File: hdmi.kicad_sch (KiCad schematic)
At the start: 46 parts, among them Q3 NVJD4401NT1G, U15 TPD4E05U06QDQARQ1, U17 TPD4E05U06QDQARQ1, U18 TPD4E05U06QDQARQ1, U21 SN75DP159_VQFN, U22 SN74AVC2T245_UQFN, U23 SN74LVC1T45YZPR, U25 NTS0104UK

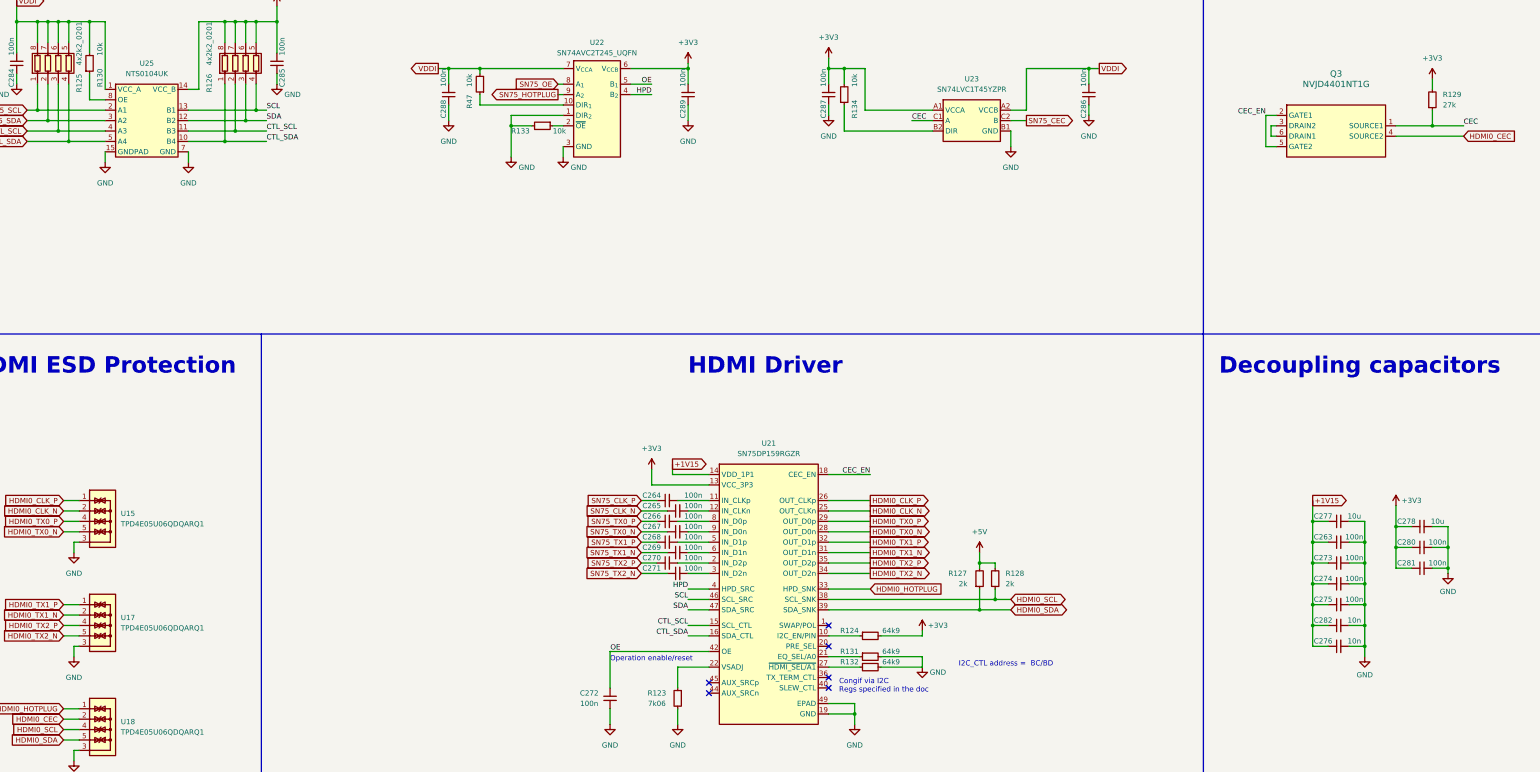
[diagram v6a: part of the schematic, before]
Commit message: [#54899] Clean duplicated components
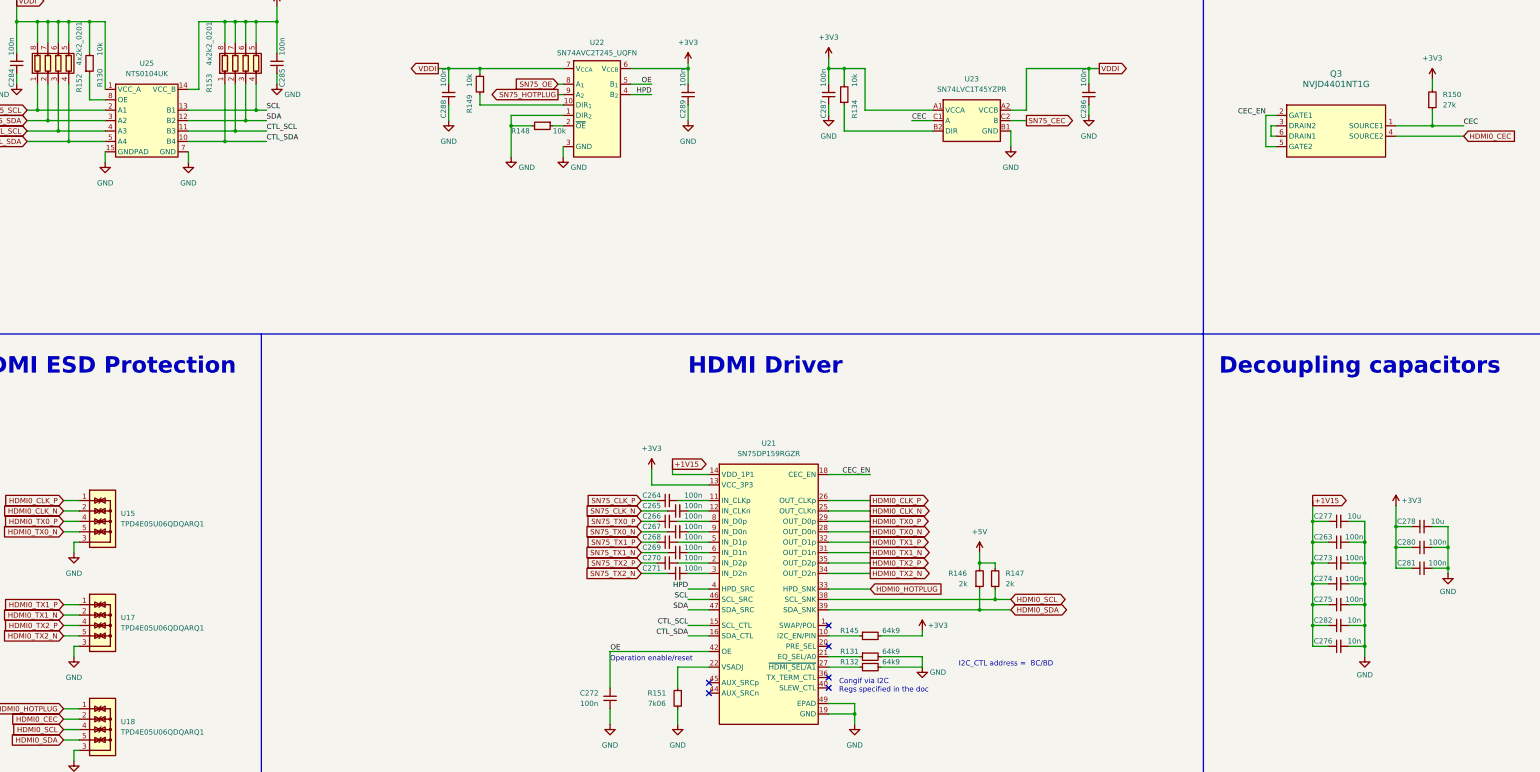
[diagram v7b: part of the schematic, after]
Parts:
- removed R123: 7k06, antmicro-footprints:R_0402_1005Metric, symbol antmicroResistors0402:R_7k06_0402
- removed R124: R_64k9_0402, antmicro-footprints:R_0402_1005Metric, symbol antmicroResistors0402:R_64k9_0402
- removed R125, R126: R_4x2k2_0201_array, antmicro-footprints:R_Array_4x0201_Panasonic_EXB18V, symbol antmicroResistorNetworksArrays:R_4x2k2_0201_array
- removed R127, R128: R_2k_0402, antmicro-footprints:R_0402_1005Metric, symbol antmicroResistors0402:R_2k_0402
- removed R129: R_27k_0402, antmicro-footprints:R_0402_1005Metric, symbol antmicroResistors0402:R_27k_0402
- removed R133, R47: R_10k_0402, antmicro-footprints:R_0402_1005Metric, symbol antmicroResistors0402:R_10k_0402
- added R145: R_64k9_0402, antmicro-footprints:R_0402_1005Metric, symbol antmicroResistors0402:R_64k9_0402
- added R146, R147: R_2k_0402, antmicro-footprints:R_0402_1005Metric, symbol antmicroResistors0402:R_2k_0402
- added R148, R149: R_10k_0402, antmicro-footprints:R_0402_1005Metric, symbol antmicroResistors0402:R_10k_0402
- added R150: R_27k_0402, antmicro-footprints:R_0402_1005Metric, symbol antmicroResistors0402:R_27k_0402
- added R151: 7k06, antmicro-footprints:R_0402_1005Metric, symbol antmicroResistors0402:R_7k06_0402
- added R152, R153: R_4x2k2_0201_array, antmicro-footprints:R_Array_4x0201_Panasonic_EXB18V, symbol antmicroResistorNetworksArrays:R_4x2k2_0201_array
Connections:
- net +3V3: now also R145.2, R150.2, R153.5 (R4.2), R153.6 (R3.2), R153.7 (R2.2), R153.8 (R1.2)
- net +5V: now also R146.2, R147.2
- net CEC: now also R150.1
- net CTL_SCL: now also R153.2 (R2.1)
- net CTL_SDA: now also R153.1 (R1.1)
- net GND: now also R148.2, R151.2
- net HDMI0_SCL: now also R147.1
- net HDMI0_SDA: now also R146.1
- net SCL: now also R153.4 (R4.1)
- net SDA: now also R153.3 (R3.1)
- net SN75_CTL_SCL: now also R152.3 (R3.1)
- net SN75_CTL_SDA: now also R152.4 (R4.1)
- net SN75_SCL: now also R152.1 (R1.1)
- net SN75_SDA: now also R152.2 (R2.1)
- net VDDI: now also R149.2, R152.5 (R4.2), R152.6 (R3.2), R152.7 (R2.2), R152.8 (R1.2)
- net at U21.10 (I2C_EN/PIN): now also R145.1
- net at U21.22 (VSADJ): now also R151.1
- net at U22.2 (~{OE}): now also R148.1
- net at U22.10 (DIR_{1}): now also R149.1

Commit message: [#54899] Re-annotate components
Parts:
- renumbered C284 to C225, C285 to C226, C288 to C227, C272 to C228, C264 to C229, C266 to C230, C268 to C231, C270 to C232, C265 to C233, C267 to C234, C269 to C235, C271 to C236, C289 to C237, C287 to C238, C286 to C239, C277 to C240, C263 to C241, C273 to C242, C274 to C243, C275 to C244, C282 to C245, C276 to C246, C278 to C247, C280 to C248, C281 to C249, Q3 to Q1, R152 to R124, R130 to R125, R153 to R126, R149 to R127, R148 to R128, R151 to R129, R134 to R130, R145 to R131, R131 to R132, R132 to R133, R146 to R134, R147 to R135, R150 to R136, U15 to U18, U17 to U19, U18 to U20, U25 to U21, U21 to U23, U23 to U24
